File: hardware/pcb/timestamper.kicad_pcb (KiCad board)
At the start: 2 copper layers, 75 x 100 mm, 110 parts, among them J1 Conn_Coaxial, J2 Conn_Coaxial, J3 Conn_Coaxial, J4 JTAG, J5 ISP, J6 Conn_Coaxial, J7 Micro_usb_B, U1 AP1117-33, U10 ATMEGA328-AU, U11 74HC04, U2 TLV71318PDBV, U3 CDCE925, U4 USBLC6-2SC6, U5 74AHC1G14, U6 74AHC1G14, U7 LMV7219?, U8 CH340G, U9 XC9572XL-VQ44, Y1 12MHz, Y2 8MHz

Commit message: backup
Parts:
- J7: value Micro_usb_B -> USB_B_Micro
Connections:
- J7 pad 6: (no net) -> GND
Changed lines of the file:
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@@
-(kicad_pcb (version 4) (host pcbnew 4.0.7-e2-6376~58~ubuntu16.04.1)
+(kicad_pcb (version 20171130) (host pcbnew 5.0.2-bee76a0~70~ubuntu16.04.1)
   (general
-    (links 278)
-    (no_connects 139)
-    (area 49.924999 49.924999 125.075001 150.075001)
     (thickness 1.6)
     (drawings 4)
@@
     (47 F.CrtYd user)
     (48 B.Fab user)
-    (49 F.Fab user)
+    (49 F.Fab user hide)
   )
   (setup
-    (last_trace_width 0.254)
+    (last_trace_width 0.25)
     (user_trace_width 0.254)
     (user_trace_width 0.381)
@@
     (pad_drill 0)
     (pad_to_mask_clearance 0.2)
+    (solder_mask_min_width 0.25)
     (aux_axis_origin 0 0)
     (visible_elements FFFEFF7F)
@@
       (layerselection 0x00030_80000001)
       (usegerberextensions false)
+      (usegerberattributes false)
+      (usegerberadvancedattributes false)
+      (creategerberjobfile false)
       (excludeedgelayer true)
       (linewidth 0.100000)
@@
       (hpglpennumber 1)
       (hpglpenspeed 20)
-      (hpglpendiameter 15)
-      (hpglpenoverlay 2)
+      (hpglpendiameter 15.000000)
       (psnegative false)
       (psa4output false)
@@
     (tags TSOT-23-5)
     (attr smd)
-    (fp_text reference U7 (at 0 2.49 450) (layer F.SilkS)
+    (fp_text reference U7 (at 0 2.49 90) (layer F.SilkS)
       (effects (font (size 1 1) (thickness 0.15)))
     )
@@
       (effects (font (size 1 1) (thickness 0.15)))
     )
-    (fp_text user %R (at -0.086 -0.11 360) (layer F.Fab)
+    (fp_text user %R (at -0.086 -0.11) (layer F.Fab)
       (effects (font (size 0.5 0.5) (thickness 0.075)))
     )
@@
     (tags "smd diode")
     (attr smd)
-    (fp_text reference D2 (at -2.54 0 450) (layer F.SilkS)
+    (fp_text reference D2 (at -2.54 0 90) (layer F.SilkS)
       (effects (font (size 1 1) (thickness 0.15)))
     )
@@
       (net 1 GND))
     (model ${KISYS3DMOD}/Socket_Strips.3dshapes/Socket_Strip_Straight_2x05_Pitch2.54mm.wrl
-      (at (xyz -0.05 -0.2 0))
+      (offset (xyz -1.269999980926514 -5.079999923706055 0))
       (scale (xyz 1 1 1))
       (rotate (xyz 0 0 270))
@@
       (net 1 GND))
     (model ${KISYS3DMOD}/Socket_Strips.3dshapes/Socket_Strip_Straight_2x03_Pitch2.54mm.wrl
-      (at (xyz -0.05 -0.1 0))
+      (offset (xyz -1.269999980926514 -2.539999961853027 0))
       (scale (xyz 1 1 1))
       (rotate (xyz 0 0 270))
@@
     (tags "resistor 0603")
     (attr smd)
-    (fp_text reference R16 (at -2.7 -0.1 360) (layer F.SilkS)
+    (fp_text reference R16 (at -2.7 -0.1) (layer F.SilkS)
       (effects (font (size 1 1) (thickness 0.15)))
     )
@@
       (effects (font (size 1 1) (thickness 0.15)))
     )
-    (fp_text value Micro_usb_B (at 0 5.01) (layer F.Fab)
+    (fp_text value USB_B_Micro (at 0 5.01) (layer F.Fab)
       (effects (font (size 1 1) (thickness 0.15)))
     )
@@
     (pad 5 smd rect (at 1.3 -1.35 90) (size 1.35 0.4) (layers F.Cu F.Paste F.Mask)
       (net 1 GND))
-    (pad 6 thru_hole oval (at -2.5 -1.35 90) (size 0.95 1.25) (drill oval 0.55 0.85) (layers *.Cu *.Mask))
-    (pad 6 thru_hole oval (at 2.5 -1.35 90) (size 0.95 1.25) (drill oval 0.55 0.85) (layers *.Cu *.Mask))
-    (pad 6 thru_hole oval (at -3.5 1.35 90) (size 1.55 1) (drill oval 1.15 0.5) (layers *.Cu *.Mask))
-    (pad 6 thru_hole oval (at 3.5 1.35 90) (size 1.55 1) (drill oval 1.15 0.5) (layers *.Cu *.Mask))
+    (pad 6 thru_hole oval (at -2.5 -1.35 90) (size 0.95 1.25) (drill oval 0.55 0.85) (layers *.Cu *.Mask)
+      (net 1 GND))
+    (pad 6 thru_hole oval (at 2.5 -1.35 90) (size 0.95 1.25) (drill oval 0.55 0.85) (layers *.Cu *.Mask)
+      (net 1 GND))
+    (pad 6 thru_hole oval (at -3.5 1.35 90) (size 1.55 1) (drill oval 1.15 0.5) (layers *.Cu *.Mask)
+      (net 1 GND))
+    (pad 6 thru_hole oval (at 3.5 1.35 90) (size 1.55 1) (drill oval 1.15 0.5) (layers *.Cu *.Mask)
+      (net 1 GND))
   )
   (module Connect:1pin (layer F.Cu)

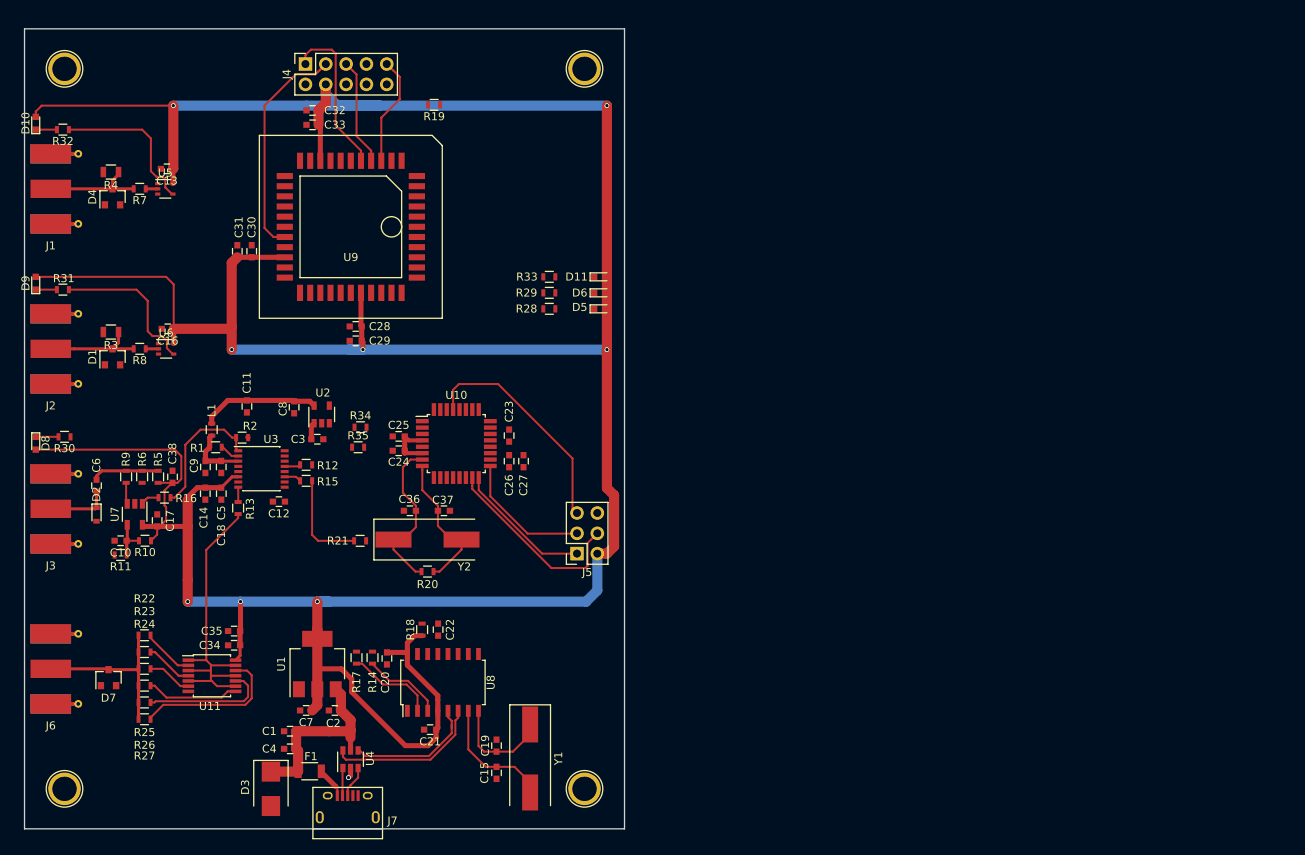
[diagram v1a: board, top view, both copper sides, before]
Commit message: Updated R and C footprints
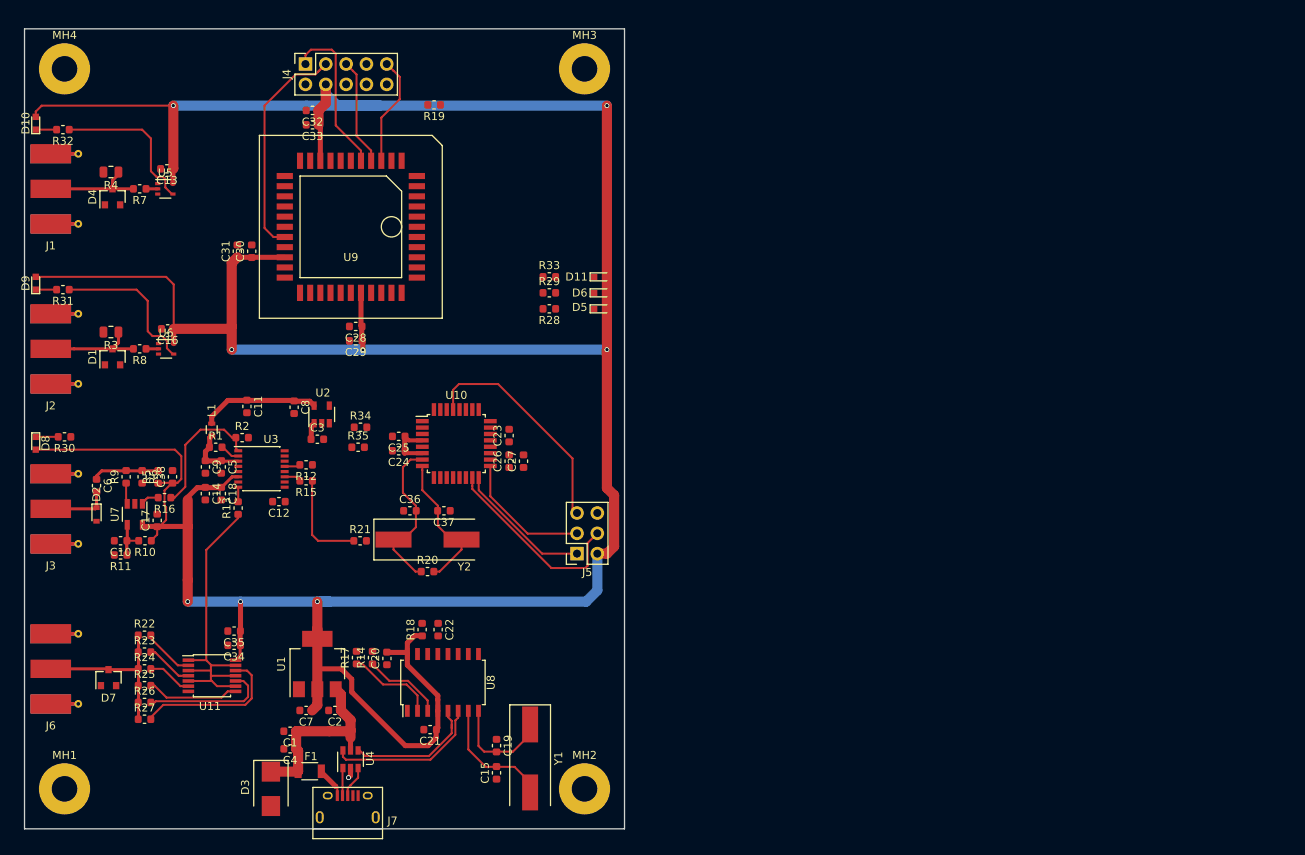
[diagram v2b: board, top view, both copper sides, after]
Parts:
- C1, C10, C11, C12, C13, C14, C15, C16, C17, C18, C19, C2, C20, C21, C22, C23, C24, C25, C26, C27, C28, C29, C3, C30, C31, C32, C33, C34, C35, C36, C37, C38, C4, C5, C6, C7, C8, C9: footprint Capacitors_SMD:C_0603 -> Capacitor_SMD:C_0603_1608Metric
- MH1, MH2, MH3, MH4: footprint Connect:1pin -> MountingHole:MountingHole_3.2mm_M3_Pad
- R1, R10, R11, R12, R13, R14, R15, R16, R17, R18, R19, R2, R20, R21, R22, R23, R24, R25, R26, R27, R28, R29, R30, R31, R32, R33, R34, R35, R5, R6, R7, R8, R9: footprint Resistors_SMD:R_0603 -> Resistor_SMD:R_0603_1608Metric
- R3, R4: footprint Resistors_SMD:R_0805 -> Resistor_SMD:R_0805_2012Metric

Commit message: Updated all footprints
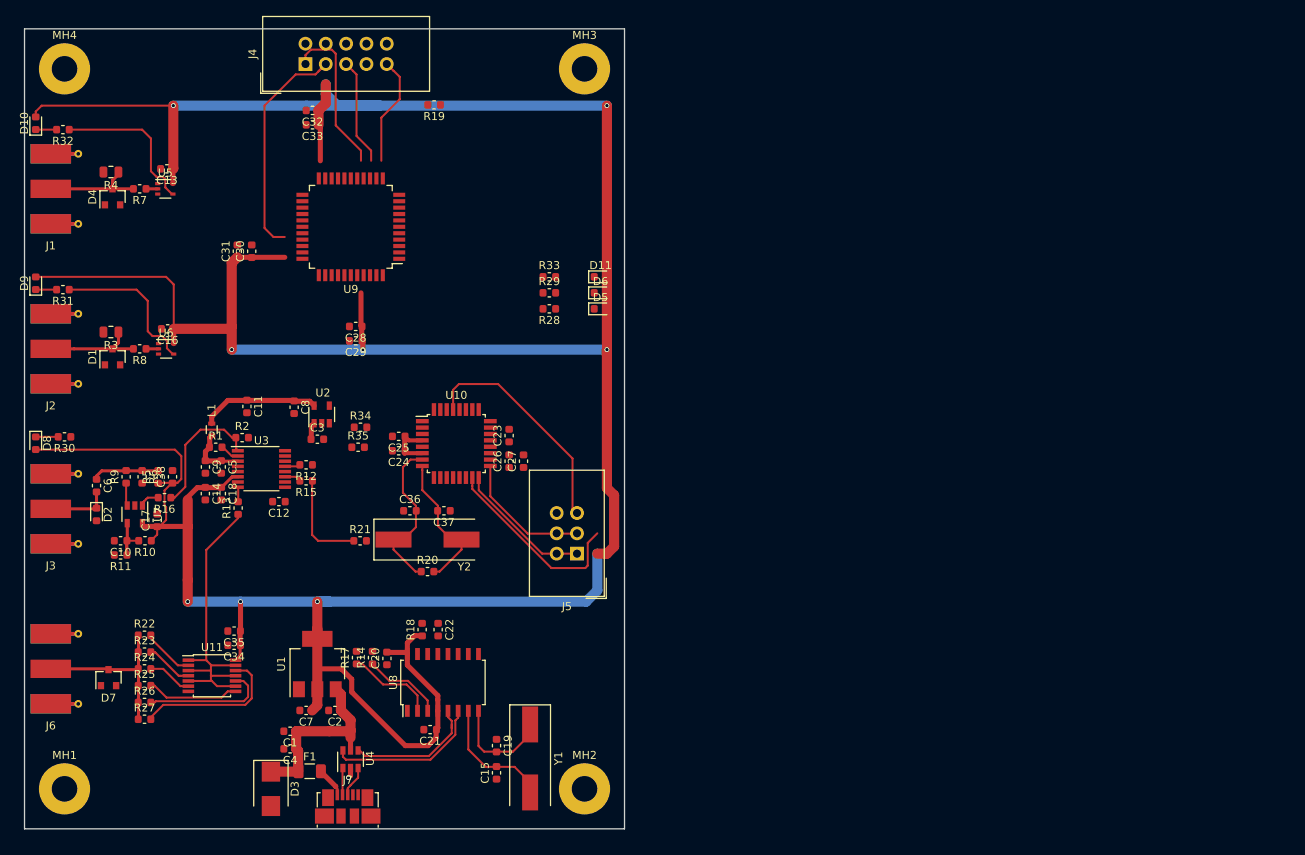
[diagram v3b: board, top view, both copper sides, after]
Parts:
- D1, D4, D7: footprint Diodes_SMD:D_SOT-23_ANK -> Diode_SMD:D_SOT-23_ANK
- D10, D11, D5, D6, D8, D9: footprint LEDs:LED_0603 -> LED_SMD:LED_0603_1608Metric
- D2: footprint Diodes_SMD:D_0603 -> Diode_SMD:D_0603_1608Metric
- D3: footprint Diodes_SMD:D_SMB -> Diode_SMD:D_SMB
- F1: footprint Resistors_SMD:R_1206 -> Resistor_SMD:R_1206_3216Metric
- J4: footprint Socket_Strips:Socket_Strip_Straight_2x05_Pitch2.54mm -> Connector_IDC:IDC-Header_2x05_P2.54mm_Vertical
- J5: footprint Socket_Strips:Socket_Strip_Straight_2x03_Pitch2.54mm -> Connector_IDC:IDC-Header_2x03_P2.54mm_Vertical
- J7: footprint Connect:USB_Micro-B -> Connector_USB:USB_Micro-B_Molex_47346-0001
- U1: footprint TO_SOT_Packages_SMD:SOT-223 -> Package_TO_SOT_SMD:SOT-223-3_TabPin2
- U10: footprint Housings_QFP:TQFP-32_7x7mm_Pitch0.8mm -> Package_QFP:TQFP-32_7x7mm_P0.8mm
- U11: footprint Housings_SSOP:TSSOP-14_4.4x5mm_Pitch0.65mm -> Package_SO:TSSOP-14_4.4x5mm_P0.65mm
- U2: footprint TO_SOT_Packages_SMD:SOT-23-5 -> Package_TO_SOT_SMD:SOT-23-5
- U3: footprint Housings_SSOP:SSOP-16_4.4x5.2mm_Pitch0.65mm -> Package_SO:TSSOP-16_4.4x5mm_P0.65mm
- U4: footprint TO_SOT_Packages_SMD:SOT-23-6 -> Package_TO_SOT_SMD:SOT-23-6
- U5, U6: footprint TO_SOT_Packages_SMD:SOT-353_SC-70-5 -> Package_TO_SOT_SMD:SOT-353_SC-70-5
- U7: footprint TO_SOT_Packages_SMD:TSOT-23-5 -> Package_TO_SOT_SMD:SOT-23-5
- U8: footprint Housings_SOIC:SOIC-16W_5.3x10.2mm_Pitch1.27mm -> Package_SO:SOIC-16W_5.3x10.2mm_P1.27mm
- U9: footprint SMD_Packages:PLCC-44 -> Package_QFP:PQFP-44_10x10mm_P0.8mm

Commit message: Finished most of routing
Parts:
- Y1, Y2: footprint Crystals:Crystal_SMD_HC49-SD -> Crystal:Crystal_HC49-4H_Vertical
- moved R19 30.7 mm to (98.3, 90.1), turned to 0 degrees
- moved C32 8.27 mm to (92.8, 64.9)
- moved C33 8.27 mm to (92.8, 66.7)
- moved Y2 8.01 mm to (92.5, 112.4)
- moved C3 7.92 mm to (85.2, 93.5), turned to 90 degrees
- moved U2 7.28 mm to (82.1, 93.0), turned to 180 degrees
- moved C31 6.61 mm to (81.6, 73.5)
- moved C30 6.61 mm to (83.4, 73.5)
- moved C8 6.29 mm to (79.2, 92.9), turned to 90 degrees
- moved C36 5.60 mm to (92.9, 108.4)
- moved C37 5.60 mm to (97.1, 108.4)
- moved R20 5.59 mm to (95.0, 116.3)
- moved R21 4.81 mm to (87.9, 111.4), turned to 270 degrees
- moved C28 4.74 mm to (88.2, 83.7)
- moved C29 4.74 mm to (88.2, 85.5)
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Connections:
- C3 pad 1: +5V -> +3V3
- R31 pad 1: /CAPTURE_N -> /LED_D9
- R32 pad 1: /PPS_N -> /LED_D10
- U2 pad 1: +5V -> +3V3
- U2 pad 3: +5V -> +3V3
- U9 pad 1: /CAPTURE_N -> /CPLD_RST_CAPT
- U9 pad 12: /SCLK -> Net-(U9-Pad12)
- U9 pad 13: /CPLD_CE_N -> Net-(U9-Pad13)
- U9 pad 16: /CPLD_INT -> Net-(U9-Pad16)
- U9 pad 18: /MISO -> Net-(U9-Pad18)
- U9 pad 2: Net-(U9-Pad2) -> /CPLD_CE_N
- U9 pad 20: /MOSI -> Net-(U9-Pad20)
- U9 pad 29: Net-(U9-Pad29) -> /PPS_N
- U9 pad 3: Net-(U9-Pad3) -> /CPLD_INT
- U9 pad 30: Net-(U9-Pad30) -> /LED_D10
- U9 pad 31: Net-(U9-Pad31) -> /LED_D9
- U9 pad 32: Net-(U9-Pad32) -> /CAPTURE_N
- U9 pad 44: /PPS_N -> Net-(U9-Pad44)
- U9 pad 5: Net-(U9-Pad5) -> /MOSI
- U9 pad 6: Net-(U9-Pad6) -> /SCLK
- U9 pad 7: Net-(U9-Pad7) -> /MISO
- U9 pad 8: /CPLD_RST_CAPT -> Net-(U9-Pad8)
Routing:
- net /USBUART_RX: track 0.00 -> 65.0 mm, vias 0 -> 3
- net /USBUART_TX: track 0.00 -> 63.4 mm, vias 0 -> 3
- net /SCLK: track 16.6 -> 71.4 mm
- net /MOSI: track 24.6 -> 69.2 mm, vias 0 -> 1
- net +3V3: track 463.7 -> 504.4 mm, vias 8 -> 17
- net /CPLD_HB: track 0.00 -> 40.6 mm
- net /LED_D10: track 0.00 -> 40.1 mm
- net /LED_D9: track 0.00 -> 32.0 mm
- net /SCL: track 0.00 -> 31.1 mm, vias 0 -> 3
- net /SDA: track 0.00 -> 30.4 mm, vias 0 -> 3
- net /MCLK_100MHZ: track 0.00 -> 28.5 mm
- net /CPU_RST_N: track 28.6 -> 55.6 mm, vias 0 -> 2
- net /CPLD_CE_N: track 0.00 -> 23.9 mm
- net /CPLD_RST_CAPT: track 0.00 -> 22.9 mm
- net /CPLD_INT: track 0.00 -> 22.2 mm
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
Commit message: Synched pinouts between CPLD and PCB
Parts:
- added R36: R, Resistor_SMD:R_0603_1608Metric, F.Cu at (94.5, 83.2)
- moved R19 5.15 mm to (98.3, 95.2)
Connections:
- U10 pad 26: Net-(U10-Pad26) -> /CPLD_MRST_N
- U10 pad 9: /CPLD_MRST_N -> Net-(U10-Pad9)
- U9 pad 1: /CPLD_RST_CAPT -> Net-(U9-Pad1)
- U9 pad 19: /CPLD_MRST_N -> Net-(U9-Pad19)
- U9 pad 29: /PPS_N -> Net-(U9-Pad29)
- U9 pad 30: /LED_D10 -> /PPS_N
- U9 pad 31: /LED_D9 -> /LED_D10
- U9 pad 32: /CAPTURE_N -> /LED_D9
- U9 pad 33: Net-(U9-Pad33) -> /CAPTURE_N
- U9 pad 44: Net-(U9-Pad44) -> /CPLD_RST_CAPT
- U9 pad 8: Net-(U9-Pad8) -> /CPLD_MRST_N
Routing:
- net /MISO: track 17.0 -> 77.1 mm
- net GND: track 4.29 -> 54.9 mm, vias 1 -> 388
- net /CPLD_MRST_N: track 0.00 -> 29.9 mm, vias 0 -> 2
- net +3V3: track 504.4 -> 512.5 mm
- net Net-(C23-Pad1): track 0.00 -> 2.60 mm
- net /CPU_RST_N: track 55.6 -> 57.9 mm
- net /MOSI: track 69.2 -> 71.1 mm
- net /CPLD_CE_N: track 23.9 -> 22.2 mm
- net /SCLK: track 71.4 -> 72.9 mm
- net /MCLK_100MHZ: track 28.5 -> 27.4 mm
- net /USBUART_TX: track 63.4 -> 64.4 mm
- net /USBUART_RX: track 65.0 -> 65.6 mm
- added copper zone on B.Cu, net GND
- added copper zone on F.Cu, net GND

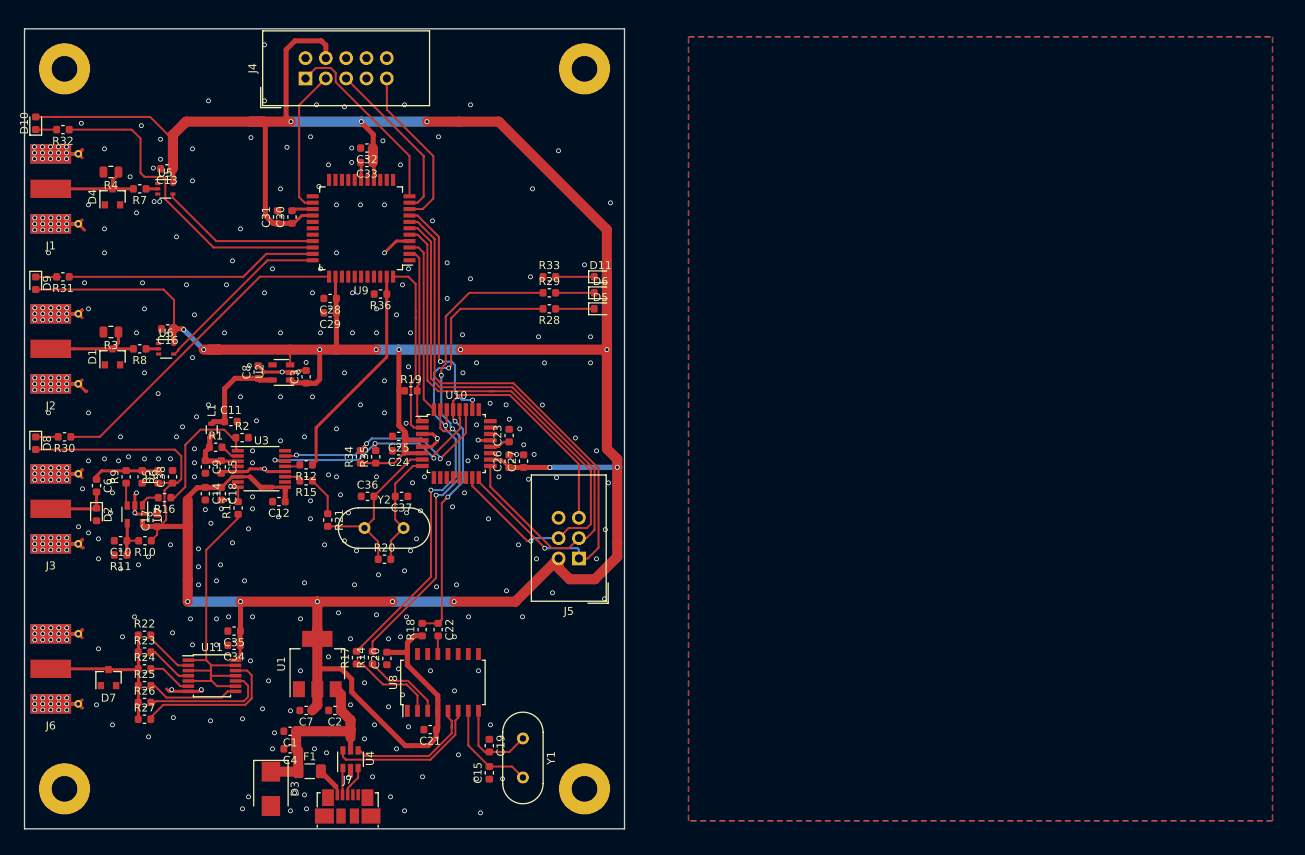
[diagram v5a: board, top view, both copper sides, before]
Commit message: Moved refdesses, added silk-screen anotations
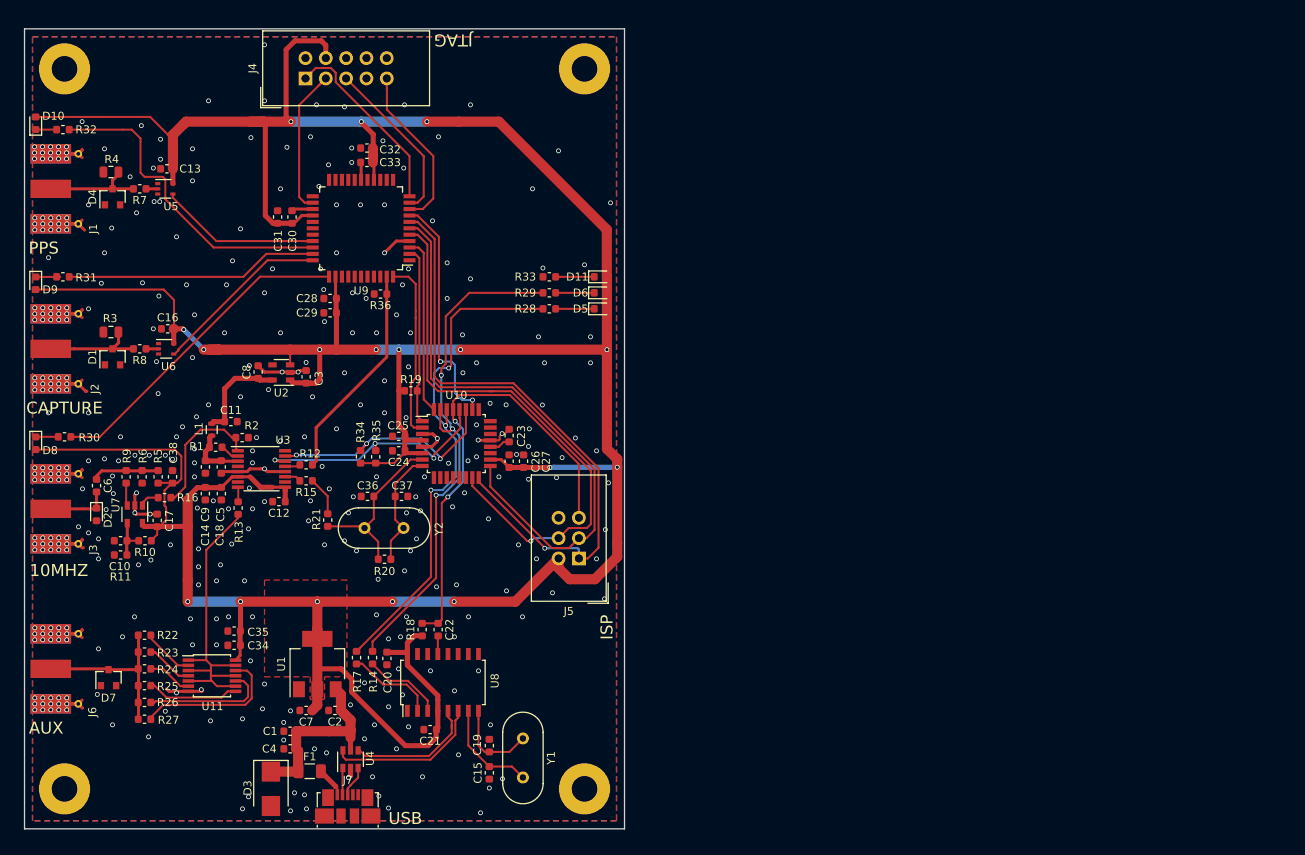
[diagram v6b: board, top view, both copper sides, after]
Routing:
- net GND: track 54.9 -> 58.1 mm, vias 388 -> 379
- added copper zone on F.Cu, net +3V3
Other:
- board text added: "10MHZ"
- board text added: "AUX"
- board text added: "CAPTURE"
- board text added: "ISP"
- board text added: "JTAG"
- board text added: "PPS"
- board text added: "USB"
